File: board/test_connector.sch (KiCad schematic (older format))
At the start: 1 part, among them P1 test_connector

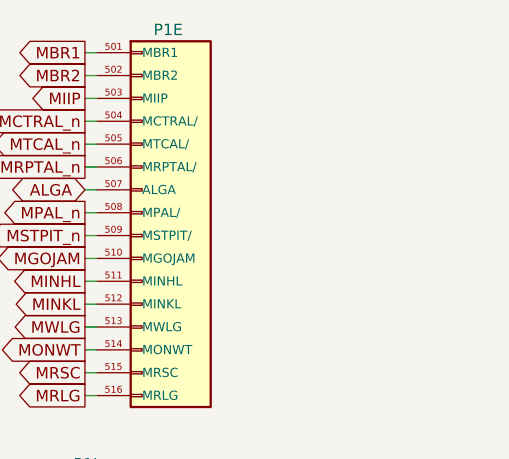
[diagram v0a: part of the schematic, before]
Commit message: Board: 5/8 of the data lanes routed
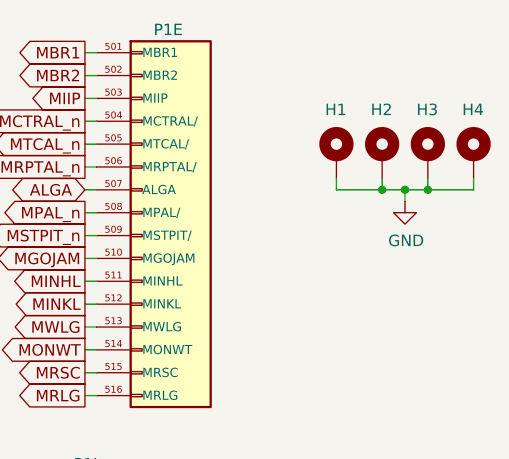
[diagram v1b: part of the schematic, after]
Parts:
- added H1, H2, H3, H4: MountingHole_Pad, agc_monitor:MountingHole_ANSI_4, symbol Mechanical:MountingHole_Pad
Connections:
- net GND: now also H1.1, H2.1, H3.1, H4.1
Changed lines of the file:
@@
 Text GLabel 5050 3850 0    50   Output ~ 0
 CTRL1
+$Comp
+L Mechanical:MountingHole_Pad H1
+U 1 1 5C9F8C28
+P 8900 2400
+F 0 "H1" H 8850 2600 50  0000 L CNN
+F 1 "MountingHole_Pad" H 9000 2360 50  0001 L CNN
+F 2 "agc_monitor:MountingHole_ANSI_4" H 8900 2400 50  0001 C CNN
+F 3 "~" H 8900 2400 50  0001 C CNN
+	1    8900 2400
+	1    0    0    -1
+$EndComp
+$Comp
+L Mechanical:MountingHole_Pad H2
+U 1 1 5C9F8D9C
+P 9100 2400
+F 0 "H2" H 9050 2600 50  0000 L CNN
+F 1 "MountingHole_Pad" H 9200 2360 50  0001 L CNN
+F 2 "agc_monitor:MountingHole_ANSI_4" H 9100 2400 50  0001 C CNN
+F 3 "~" H 9100 2400 50  0001 C CNN
+	1    9100 2400
+	1    0    0    -1
+$EndComp
+$Comp
+L Mechanical:MountingHole_Pad H3
+U 1 1 5CA02E57
+P 9300 2400
+F 0 "H3" H 9250 2600 50  0000 L CNN
+F 1 "MountingHole_Pad" H 9400 2360 50  0001 L CNN
+F 2 "agc_monitor:MountingHole_ANSI_4" H 9300 2400 50  0001 C CNN
+F 3 "~" H 9300 2400 50  0001 C CNN
+	1    9300 2400
+	1    0    0    -1
+$EndComp
+$Comp
+L Mechanical:MountingHole_Pad H4
+U 1 1 5CA02E5D
+P 9500 2400
+F 0 "H4" H 9450 2600 50  0000 L CNN
+F 1 "MountingHole_Pad" H 9600 2360 50  0001 L CNN
+F 2 "agc_monitor:MountingHole_ANSI_4" H 9500 2400 50  0001 C CNN
+F 3 "~" H 9500 2400 50  0001 C CNN
+	1    9500 2400
+	1    0    0    -1
+$EndComp
+Wire Wire Line
+	8900 2500 8900 2550
+Wire Wire Line
+	8900 2550 9100 2550
+Wire Wire Line
+	9500 2550 9500 2500
+Wire Wire Line
+	9300 2500 9300 2550
+Connection ~ 9300 2550
+Wire Wire Line
+	9300 2550 9500 2550
+Wire Wire Line
+	9100 2500 9100 2550
+Connection ~ 9100 2550
+Wire Wire Line
+	9100 2550 9200 2550
+Wire Wire Line
+	9200 2550 9200 2600
+Connection ~ 9200 2550
+Wire Wire Line
+	9200 2550 9300 2550
+$Comp
+L power:GND #PWR0178
+U 1 1 5CA35FFD
+P 9200 2600
+F 0 "#PWR0178" H 9200 2350 50  0001 C CNN
+F 1 "GND" H 9205 2427 50  0000 C CNN
+F 2 "" H 9200 2600 50  0001 C CNN
+F 3 "" H 9200 2600 50  0001 C CNN
+	1    9200 2600
+	1    0    0    -1
+$EndComp
 $EndSCHEMATC
